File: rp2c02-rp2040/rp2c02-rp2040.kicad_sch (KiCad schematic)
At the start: 23 parts, among them J1 VIDEO, J2 Si5351A, Q1 2SA937, Q2 AO3400A, SW1 RUN, U1 RP2C02, U2 74HC574N, U3 IS62C256AL, U4 Pico

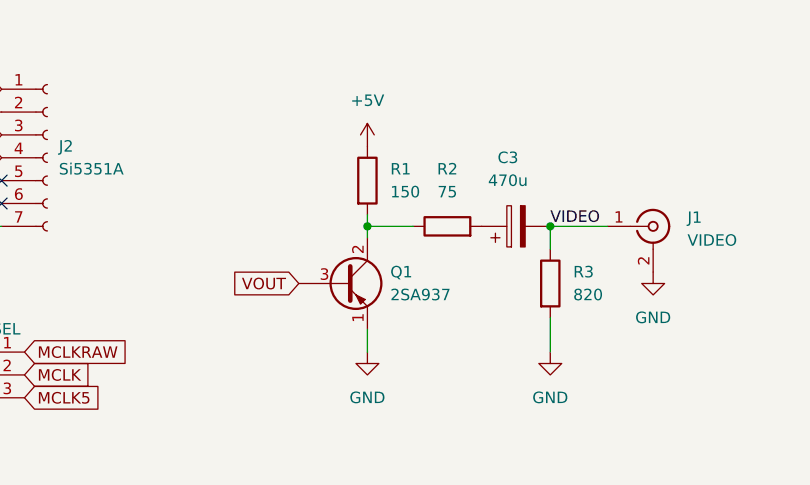
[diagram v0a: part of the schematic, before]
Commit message: レベルシフト版/レベルシフト基板追加、通常基板の2SA937ピン逆転修正
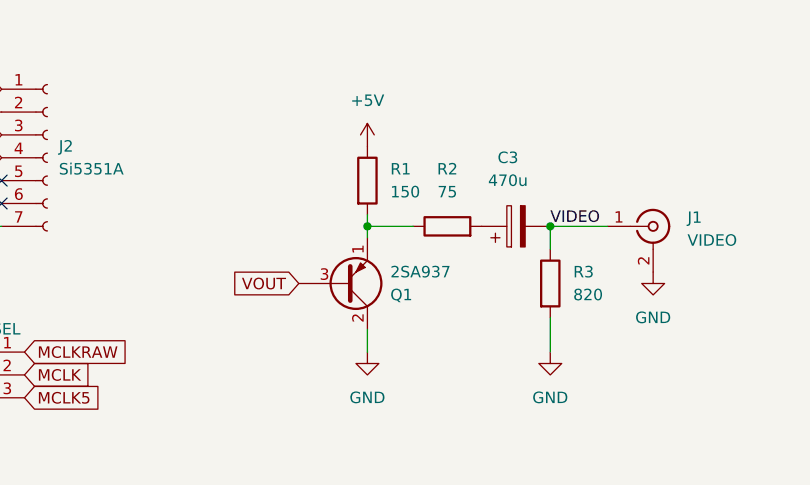
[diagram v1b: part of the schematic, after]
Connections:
- net GND: now also Q1.2 (C); no longer Q1.1 (E)
- net at R1.2, R2.1: now also Q1.1 (E); no longer Q1.2 (C)
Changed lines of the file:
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@@
 		(lib_id "Device:Q_PNP_ECB")
 		(at 92.71 158.75 0)
+		(mirror x)
 		(unit 1)
 		(exclude_from_sim no)
@@
 		(on_board yes)
 		(dnp no)
-		(fields_autoplaced yes)
 		(property "Reference" "Q1"
-			(at 97.79 157.4799 0)
+			(at 97.79 160.0201 0)
 			(effects
 				(font
@@
 		)
 		(property "Value" "2SA937"
-			(at 97.79 160.0199 0)
+			(at 97.79 157.4801 0)
 			(effects
 				(font
@@
 		)
 		(property "Footprint" "Connector_PinSocket_2.54mm:PinSocket_1x03_P2.54mm_Vertical"
-			(at 97.79 156.21 0)
+			(at 97.79 161.29 0)
 			(effects
 				(font

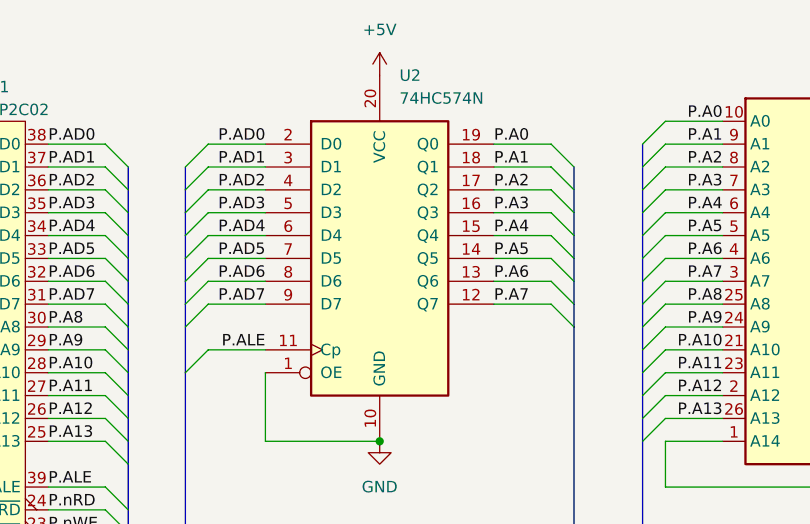
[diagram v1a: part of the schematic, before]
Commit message: 74HC573に修正
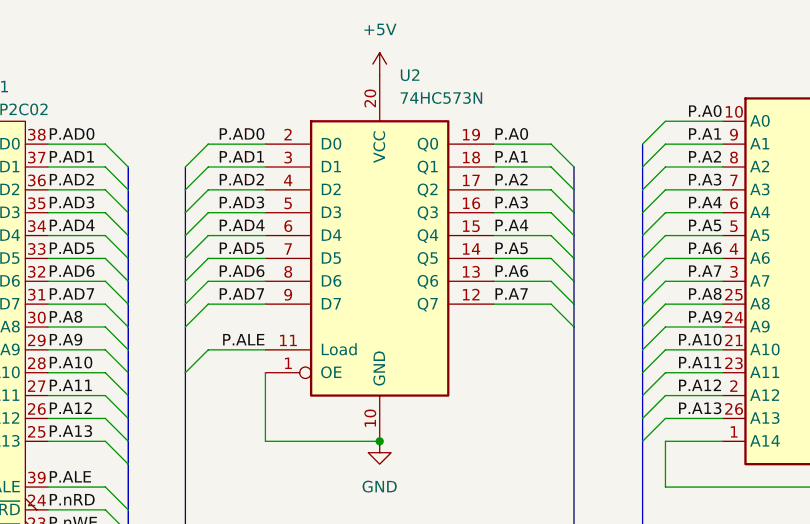
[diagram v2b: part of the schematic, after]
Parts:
- U2: value 74HC574N -> 74HC573N; symbol 74xx:74LS574 -> 74xx:74LS573
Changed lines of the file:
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@@
 	)
 	(symbol
-		(lib_id "74xx:74LS574")
+		(lib_id "74xx:74LS573")
 		(at 157.48 43.18 0)
 		(unit 1)
@@
 			)
 		)
-		(property "Value" "74HC574N"
+		(property "Value" "74HC573N"
 			(at 159.6741 25.4 0)
 			(effects
@@
 			)
 		)
-		(property "Datasheet" "http://www.ti.com/lit/gpn/sn74LS574"
+		(property "Datasheet" "74xx/74hc573.pdf"
 			(at 157.48 43.18 0)
 			(effects
@@
 			)
 		)
-		(property "Description" "8-bit Register, 3-state outputs"
+		(property "Description" "8-bit Latch 3-state outputs"
 			(at 157.48 43.18 0)
 			(effects
